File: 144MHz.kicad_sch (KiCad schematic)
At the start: 32 parts, among them J4 BWSMA-KWE-Z001, U5 GRF5604, U6 SKYA21003

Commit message: Finish up inputting things
Signed-off-by: Corey Minyard <corey@minyard.net>
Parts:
- removed C38: 680pF, Capacitor_SMD:C_0402_1005Metric_Pad0.74x0.62mm_HandSolder, symbol Device:C
- added C70: 18pF, Capacitor_SMD:C_0402_1005Metric_Pad0.74x0.62mm_HandSolder, symbol Device:C
- added C71: 1uF, Capacitor_SMD:C_0402_1005Metric_Pad0.74x0.62mm_HandSolder, symbol Device:C
- added L16: 150nH, Inductor_SMD:L_1210_3225Metric_Pad1.42x2.65mm_HandSolder, symbol Device:L
- added L20: 1uH, Inductor_SMD:L_1210_3225Metric_Pad1.42x2.65mm_HandSolder, symbol Device:L
- added R15: 350Ω, Resistor_SMD:R_0402_1005Metric, symbol Device:R
- added R17: 0Ω, Resistor_SMD:R_0402_1005Metric, symbol Device:R
- C36: value 100pF -> 680pF
- C39, C44: value 680pF -> 220pF
- C40, C43: value 12pF -> 47pF
- C41: value 12pF -> 100pF
- C42: value 12pF -> 270pF
- C45, C46: value 12pF -> 1000pF
- C47: value 12pF -> 10uF
- C48: value 12pF -> 0; now not fitted; now left out of the parts list
- L7: value 68nH -> 9.1nH
- L8: value 68nH -> 1uH
- R10: value 56K 1% -> 0Ω
- R8: value 56K 1% -> 2K 1%
- R9: value 56K 1% -> 6K 1%
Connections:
- net +5V: now also R9.1, R17.1; no longer R9.2, U5.13 (VCC1)
- net GND: now also U5.14 (GND/NC), C70.1, C71.1, R15.1
- net at C46.2, U5.15 (VENABLE2): now also R9.2; no longer R9.1
- net at C40.2, C43.2, C44.1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: now also C70.2
- net 144MHz_TX_ENABLE: now reaches U5.1 (~{VSHUTDOWN})
- net at R10.2: now also C71.2, L20.2; no longer U5.12 (BIAS)
- net at C39.1, L6.2: now also L16.2
- net at C36.2: now also L16.1, R15.2
- new net: R17.2, U5.12 (BIAS)
- new net: L20.1, U5.13 (VCC1)
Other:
- moved on the sheet: C34, C36, C39, C44, R8, R9

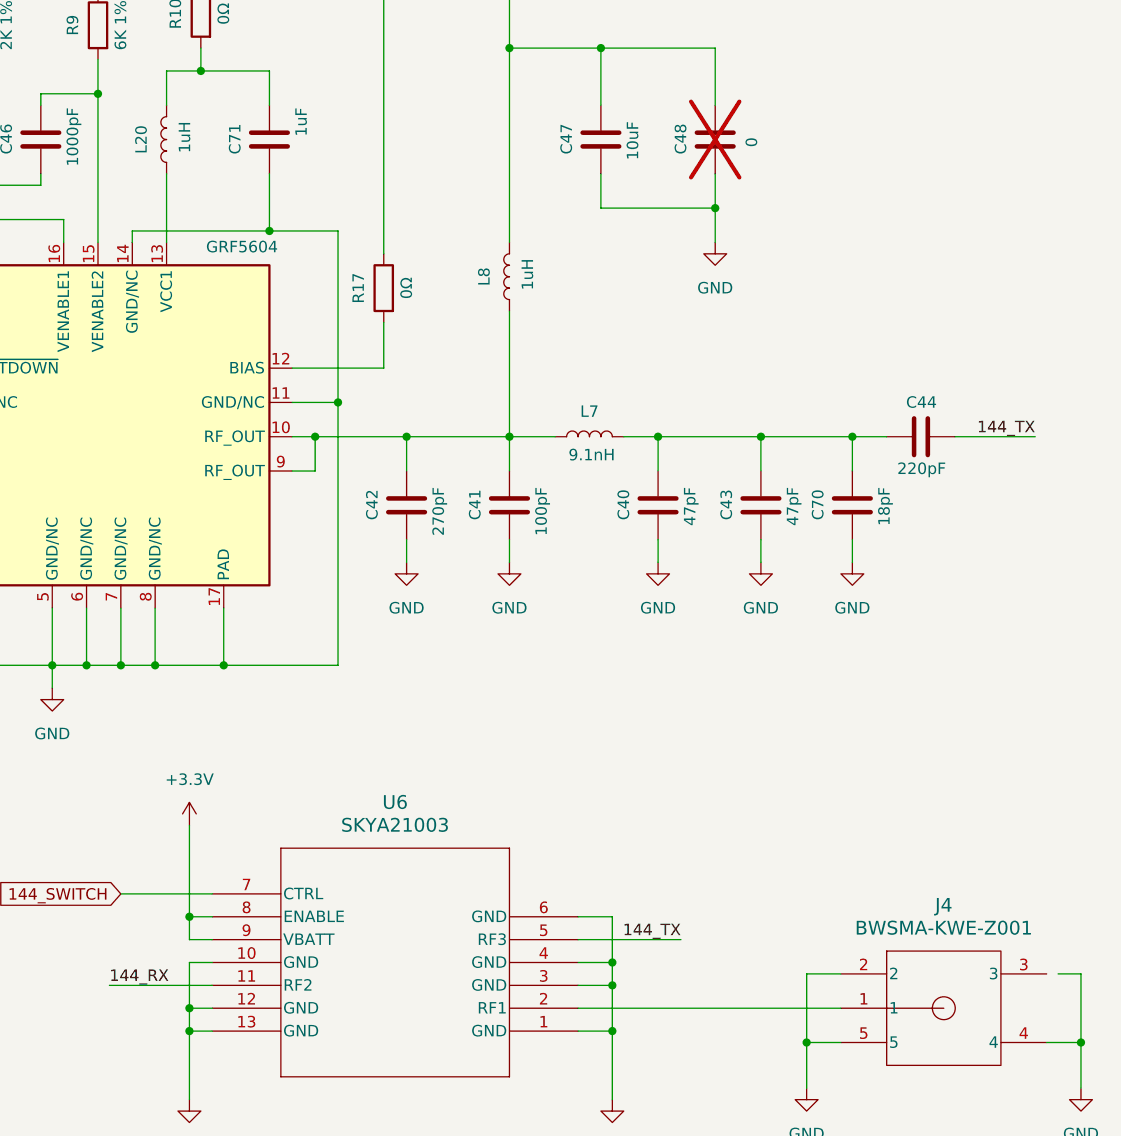
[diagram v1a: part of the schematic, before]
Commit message: Clean up schematics
Signed-off-by: Corey Minyard <corey@minyard.net>
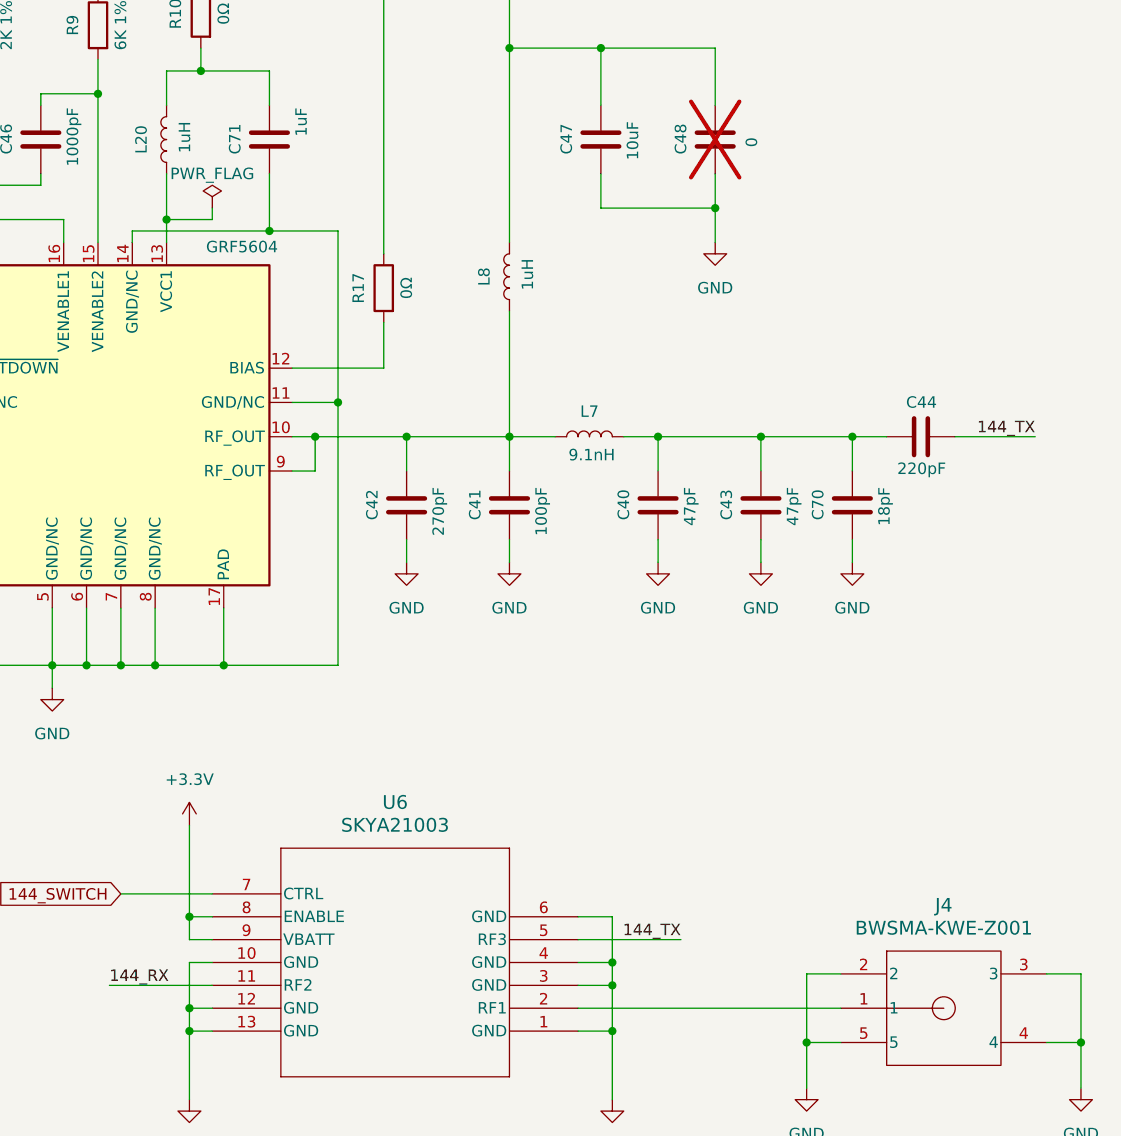
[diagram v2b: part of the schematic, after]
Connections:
- net GND: now also J4.3
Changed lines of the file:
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@@
 	)
 	(junction
+		(at 173.99 54.61)
+		(diameter 0)
+		(color 0 0 0 0)
+	)
+	(junction
 		(at 72.39 128.27)
 		(diameter 0)
@@
 	(wire
 		(pts
+			(xy 271.78 138.43) (xy 275.59 138.43)
+		)
+		(stroke
+			(width 0)
+			(type default)
+		)
+	)
+	(wire
+		(pts
 			(xy 198.12 71.12) (xy 198.12 66.04)
 		)
@@
 	(wire
 		(pts
+			(xy 179.07 53.34) (xy 179.07 54.61)
+		)
+		(stroke
+			(width 0)
+			(type default)
+		)
+	)
+	(wire
+		(pts
 			(xy 177.8 38.1) (xy 173.99 38.1)
 		)
@@
 	(wire
 		(pts
-			(xy 36.83 144.78) (xy 54.61 144.78)
+			(xy 179.07 54.61) (xy 173.99 54.61)
 		)
 		(stroke
@@
 	(wire
 		(pts
-			(xy 162.56 54.61) (xy 162.56 57.15)
+			(xy 36.83 144.78) (xy 54.61 144.78)
 		)
 		(stroke
@@
 	(wire
 		(pts
-			(xy 275.59 138.43) (xy 273.05 138.43)
+			(xy 162.56 54.61) (xy 162.56 57.15)
 		)
 		(stroke
@@
 	(wire
 		(pts
+			(xy 173.99 49.53) (xy 173.99 54.61)
+		)
+		(stroke
+			(width 0)
+			(type default)
+		)
+	)
+	(wire
+		(pts
 			(xy 88.9 78.74) (xy 92.71 78.74)
 		)
@@
 	(wire
 		(pts
+			(xy 173.99 54.61) (xy 173.99 57.15)
+		)
+		(stroke
+			(width 0)
+			(type default)
+		)
+	)
+	(wire
+		(pts
 			(xy 222.25 35.56) (xy 222.25 41.91)
 		)
@@
 	(wire
 		(pts
+			(xy 219.71 142.24) (xy 248.92 142.24)
+		)
+		(stroke
+			(width 0)
+			(type default)
+		)
+	)
+	(wire
+		(pts
 			(xy 54.61 144.78) (xy 54.61 149.86)
 		)
@@
 	(wire
 		(pts
-			(xy 173.99 49.53) (xy 173.99 57.15)
-		)
-		(stroke
-			(width 0)
-			(type default)
-		)
-	)
-	(wire
-		(pts
 			(xy 170.18 55.88) (xy 185.42 55.88)
 		)
@@
 	(wire
 		(pts
-			(xy 219.71 142.24) (xy 248.92 142.24)
-		)
-		(stroke
-			(width 0)
-			(type default)
-		)
-	)
-	(wire
-		(pts
 			(xy 234.95 35.56) (xy 222.25 35.56)
 		)
@@
 		(pin "5"
 		)
+		(instances
+			(project ""
+				(path "/23e49ab9-97e0-460a-806c-ff6f37958474/09d49814-9bff-4ecc-b3ba-584a511e3f87"
+					(reference "J4")
+					(unit 1)
+				)
+			)
+		)
 	)
 	(symbol
@@
 					(unit 1)
 				)
+			)
+		)
+	)
+	(symbol
+		(lib_id "power:PWR_FLAG")
+		(at 179.07 53.34 0)
+		(unit 1)
+		(exclude_from_sim no)
+		(in_bom yes)
+		(on_board yes)
+		(dnp no)
+		(property "Reference" "#FLG01"
+			(at 179.07 51.435 0)
+			(effects
+				(font
+					(size 1.27 1.27)
+				)
+				(hide yes)
+			)
+		)
+		(property "Value" "PWR_FLAG"
+			(at 179.07 49.53 0)
+			(effects
+				(font
+					(size 1.27 1.27)
+				)
+			)
+		)
+		(property "Footprint" ""
+			(at 179.07 53.34 0)
+			(effects
+				(font
+					(size 1.27 1.27)
+				)
+				(hide yes)
+			)
+		)
+		(property "Datasheet" "~"
+			(at 179.07 53.34 0)
+			(effects
+				(font
+					(size 1.27 1.27)
+				)
+				(hide yes)
+			)
+		)
+		(property "Description" "Special symbol for telling ERC where power comes from"
+			(at 179.07 53.34 0)
+			(effects
+				(font
+					(size 1.27 1.27)
+				)
+				(hide yes)
+			)
+		)
+		(pin "1"
+		)
+		(instances
+			(project "FSKGroundStation"
+				(path "/23e49ab9-97e0-460a-806c-ff6f37958474/09d49814-9bff-4ecc-b3ba-584a511e3f87"
+					(reference "#FLG01")
+					(unit 1)
+				)

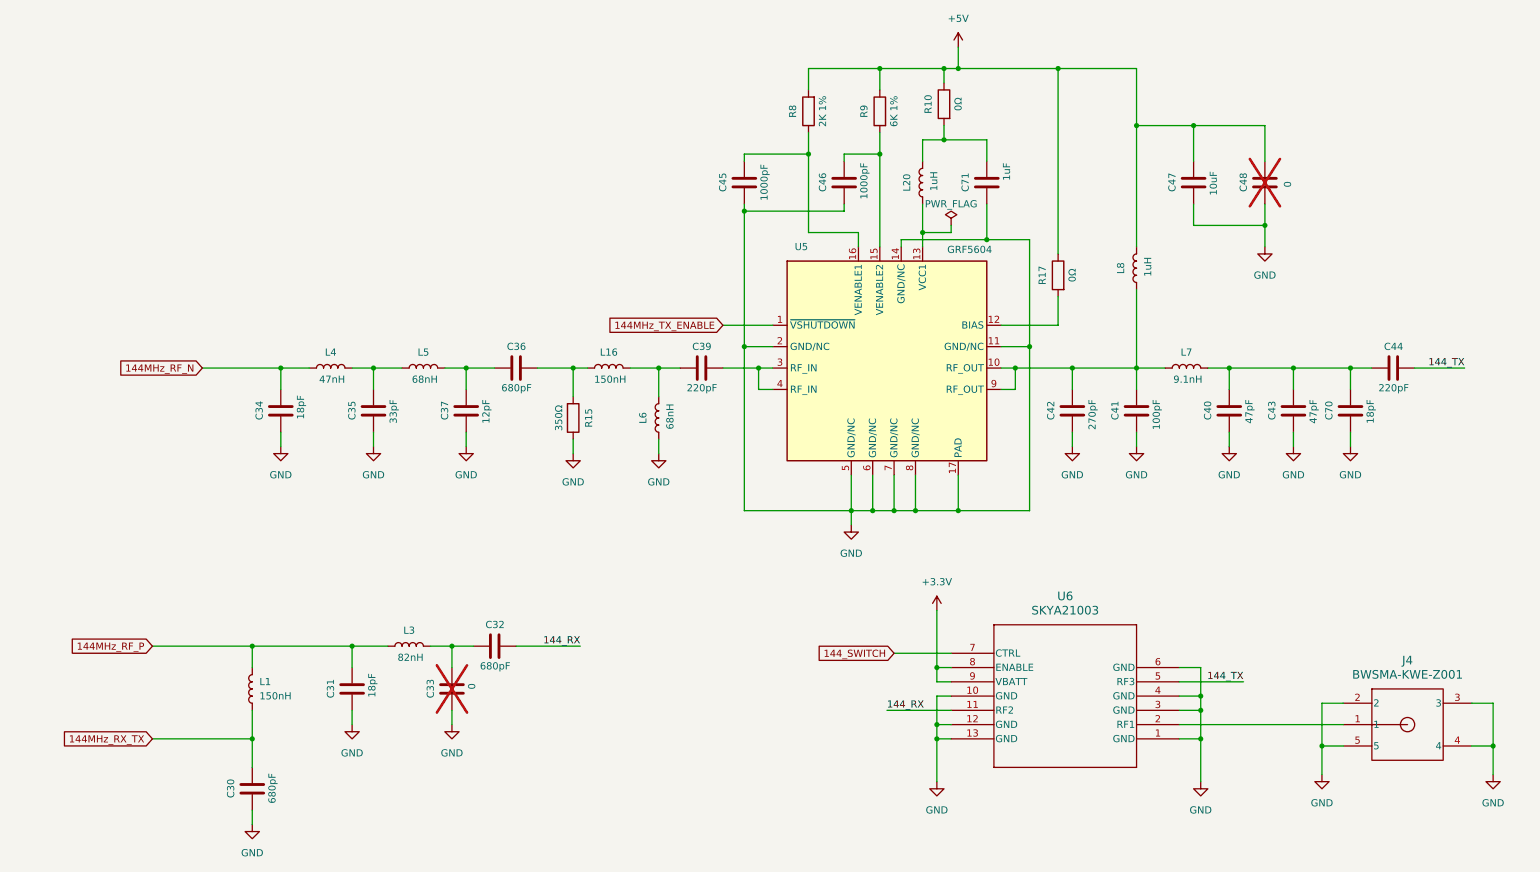
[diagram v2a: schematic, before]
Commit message: More cleanups and add some test points
Signed-off-by: Corey Minyard <corey@minyard.net>
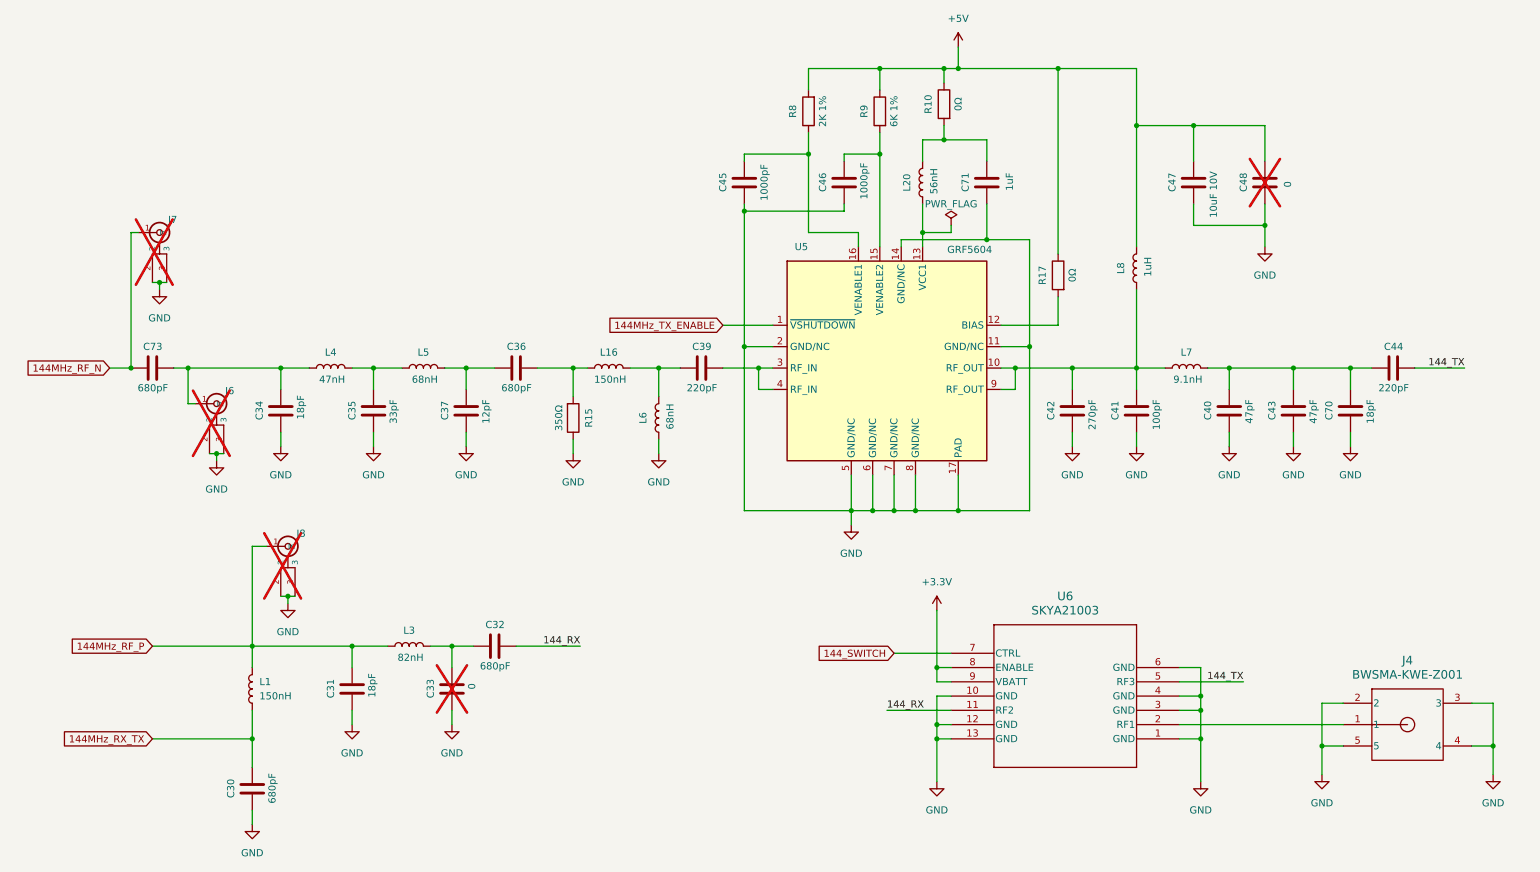
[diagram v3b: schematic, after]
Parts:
- added C73: 680pF, Capacitor_SMD:C_0402_1005Metric_Pad0.74x0.62mm_HandSolder, symbol Device:C
- added J6, J7, J8: ~, footprints:CONN1_CONUFL_TEC, symbol Local Connectors:U_FL
- C47: value 10uF -> 10uF 10V; footprint Capacitor_SMD:C_0402_1005Metric_Pad0.74x0.62mm_HandSolder -> Capacitor_SMD:C_0805_2012Metric_Pad1.18x1.45mm_HandSolder
- L1, L16: footprint Inductor_SMD:L_1210_3225Metric_Pad1.42x2.65mm_HandSolder -> Inductor_SMD:L_0805_2012Metric_Pad1.05x1.20mm_HandSolder
- L20: value 1uH -> 56nH; footprint Inductor_SMD:L_1210_3225Metric_Pad1.42x2.65mm_HandSolder -> Inductor_SMD:L_0603_1608Metric_Pad1.05x0.95mm_HandSolder
- L3, L4, L5, L6: footprint Inductor_SMD:L_1210_3225Metric_Pad1.42x2.65mm_HandSolder -> Inductor_SMD:L_0603_1608Metric_Pad1.05x0.95mm_HandSolder
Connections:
- net 144MHz_RF_N: now also C73.1, J7.1 (In); no longer C34.2, L4.1
- net 144MHz_RF_P: now also J8.1 (In)
- net GND: now also J6.2, J6.3, J7.2, J7.3, J8.2, J8.3
- new net: C34.2, C73.2, J6.1 (In), L4.1

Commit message: Add more test points
Signed-off-by: Corey Minyard <corey@minyard.net>
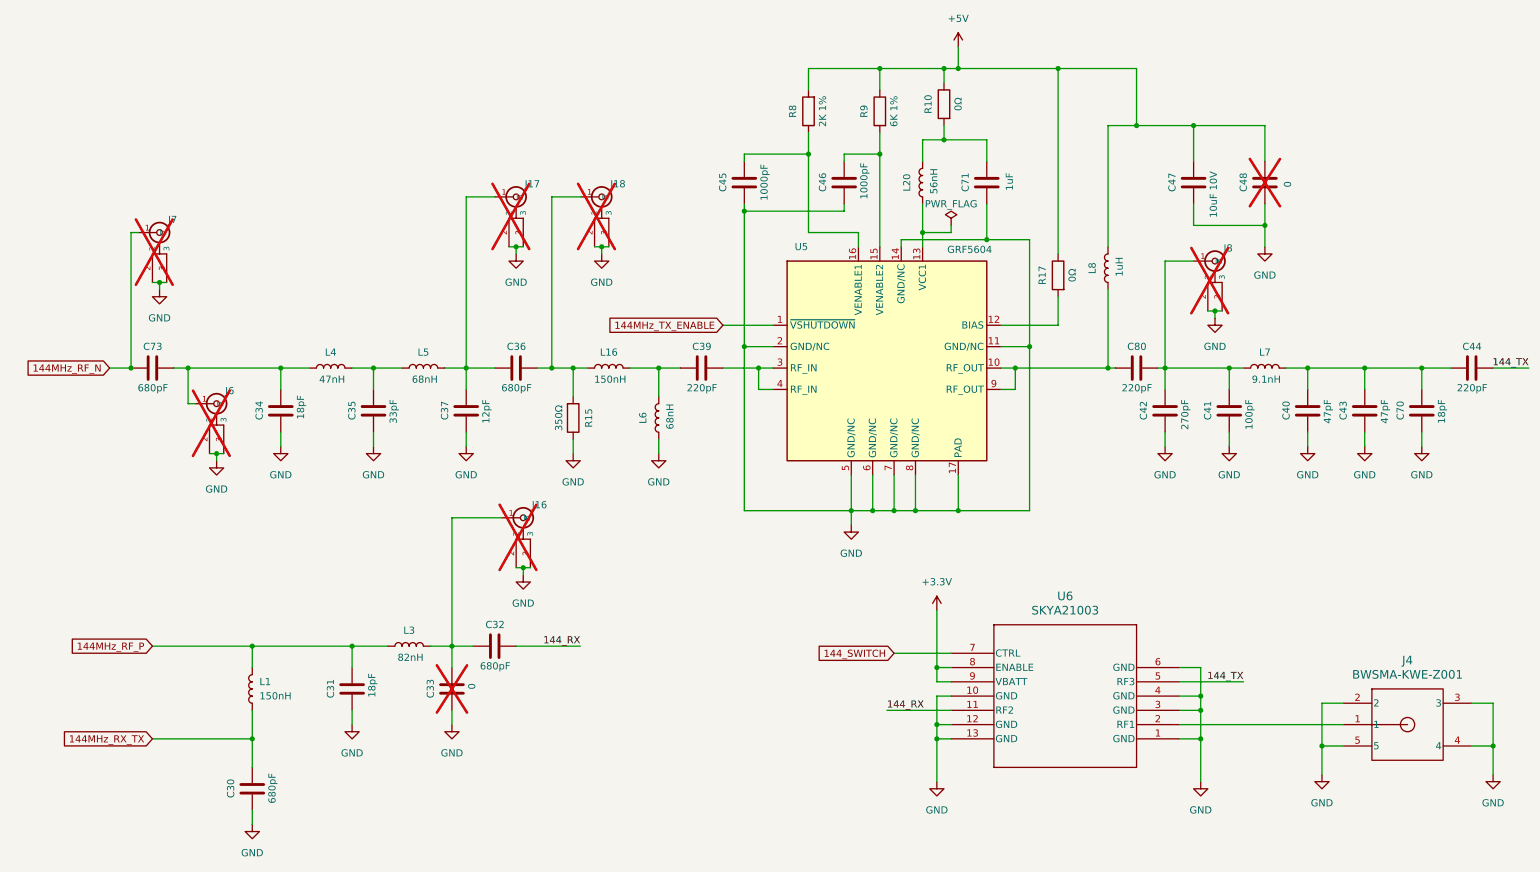
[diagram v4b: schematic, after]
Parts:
- added C80: 220pF, Capacitor_SMD:C_0402_1005Metric_Pad0.74x0.62mm_HandSolder, symbol Device:C
- added J16, J17, J18: ~, footprints:CONN1_CONUFL_TEC, symbol Local Connectors:U_FL
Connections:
- net 144MHz_RF_P: no longer J8.1 (In)
- net GND: now also J16.2, J16.3, J17.2, J17.3, J18.2, J18.3
- net at L8.1, U5.10 (RF_OUT), U5.9 (RF_OUT): now also C80.1; no longer C41.2, C42.2, L7.1
- net at C36.2, L16.1, R15.2: now also J18.1 (In)
- net at C36.1, C37.2, L5.2: now also J17.1 (In)
- net at C32.1, C33.2, L3.2: now also J16.1 (In)
- new net: C41.2, C42.2, C80.2, J8.1 (In), L7.1
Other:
- moved on the sheet: C40, C41, C42, C43, C44, C70, L7, L8

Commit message: Layout work
Signed-off-by: Corey Minyard <corey@minyard.net>
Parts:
- L7: footprint Inductor_SMD:L_1210_3225Metric_Pad1.42x2.65mm_HandSolder -> Inductor_SMD:L_0402_1005Metric_Pad0.77x0.64mm_HandSolder
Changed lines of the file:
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@@
 			)
 		)
-		(property "Footprint" "Inductor_SMD:L_1210_3225Metric_Pad1.42x2.65mm_HandSolder"
+		(property "Footprint" "Inductor_SMD:L_0402_1005Metric_Pad0.77x0.64mm_HandSolder"
 			(at 234.95 78.74 0)
 			(effects

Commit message: Finish layout
Signed-off-by: Corey Minyard <corey@minyard.net>
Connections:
- net RF_144: now reaches J4.1, U6.2 (RF1)
